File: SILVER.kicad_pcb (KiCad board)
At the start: 2 copper layers, 66 parts, among them J1 Conn_02x22, J2 Conn_02x22, J3 MPU6050, J4 MotorL, J5 motorR, J6 XT60-M, J7 STLINK, Q1 FCD600N60Z, Q2 FCD600N60Z, U1 VNH5019A-E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

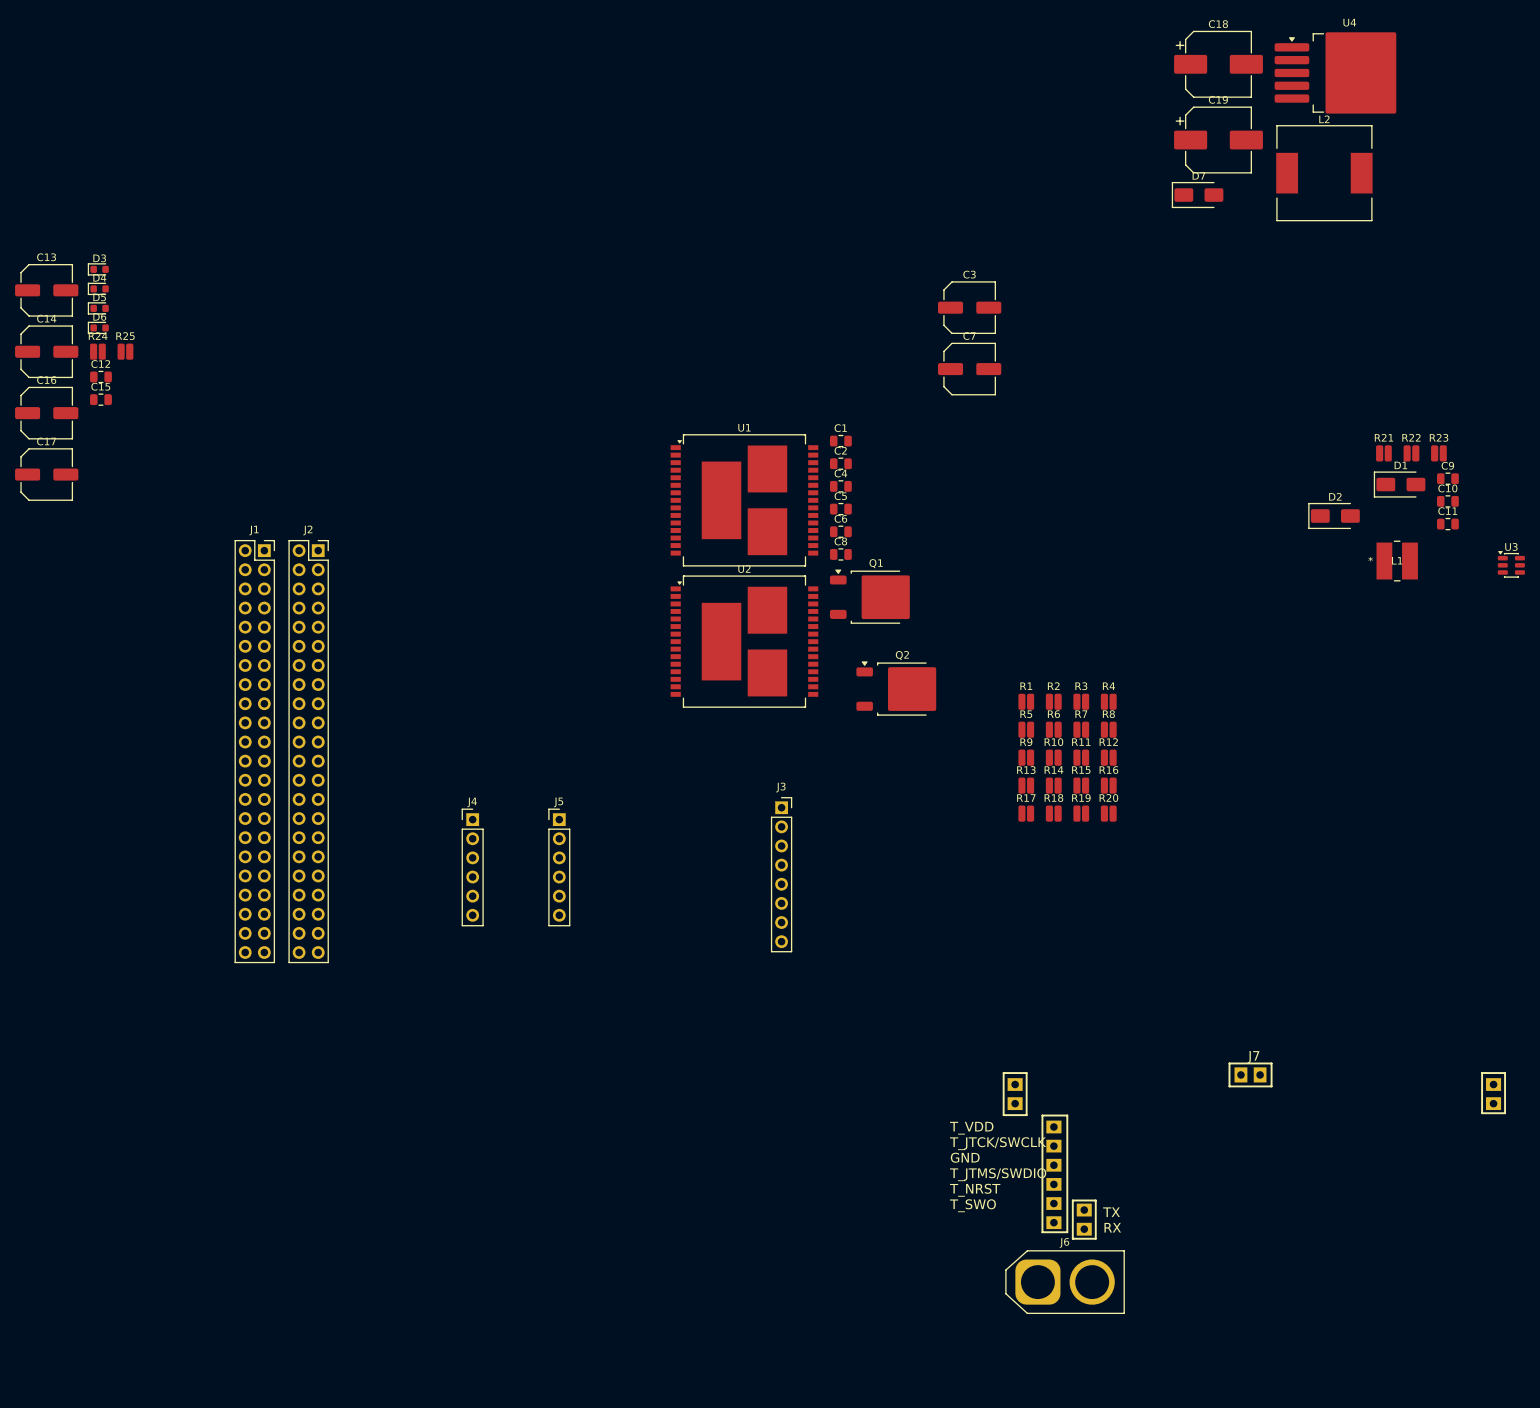
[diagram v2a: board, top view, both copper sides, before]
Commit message: feat: Update main project schematic and PCB with new component footprint and connector details, and add new RB141C1100 component files.
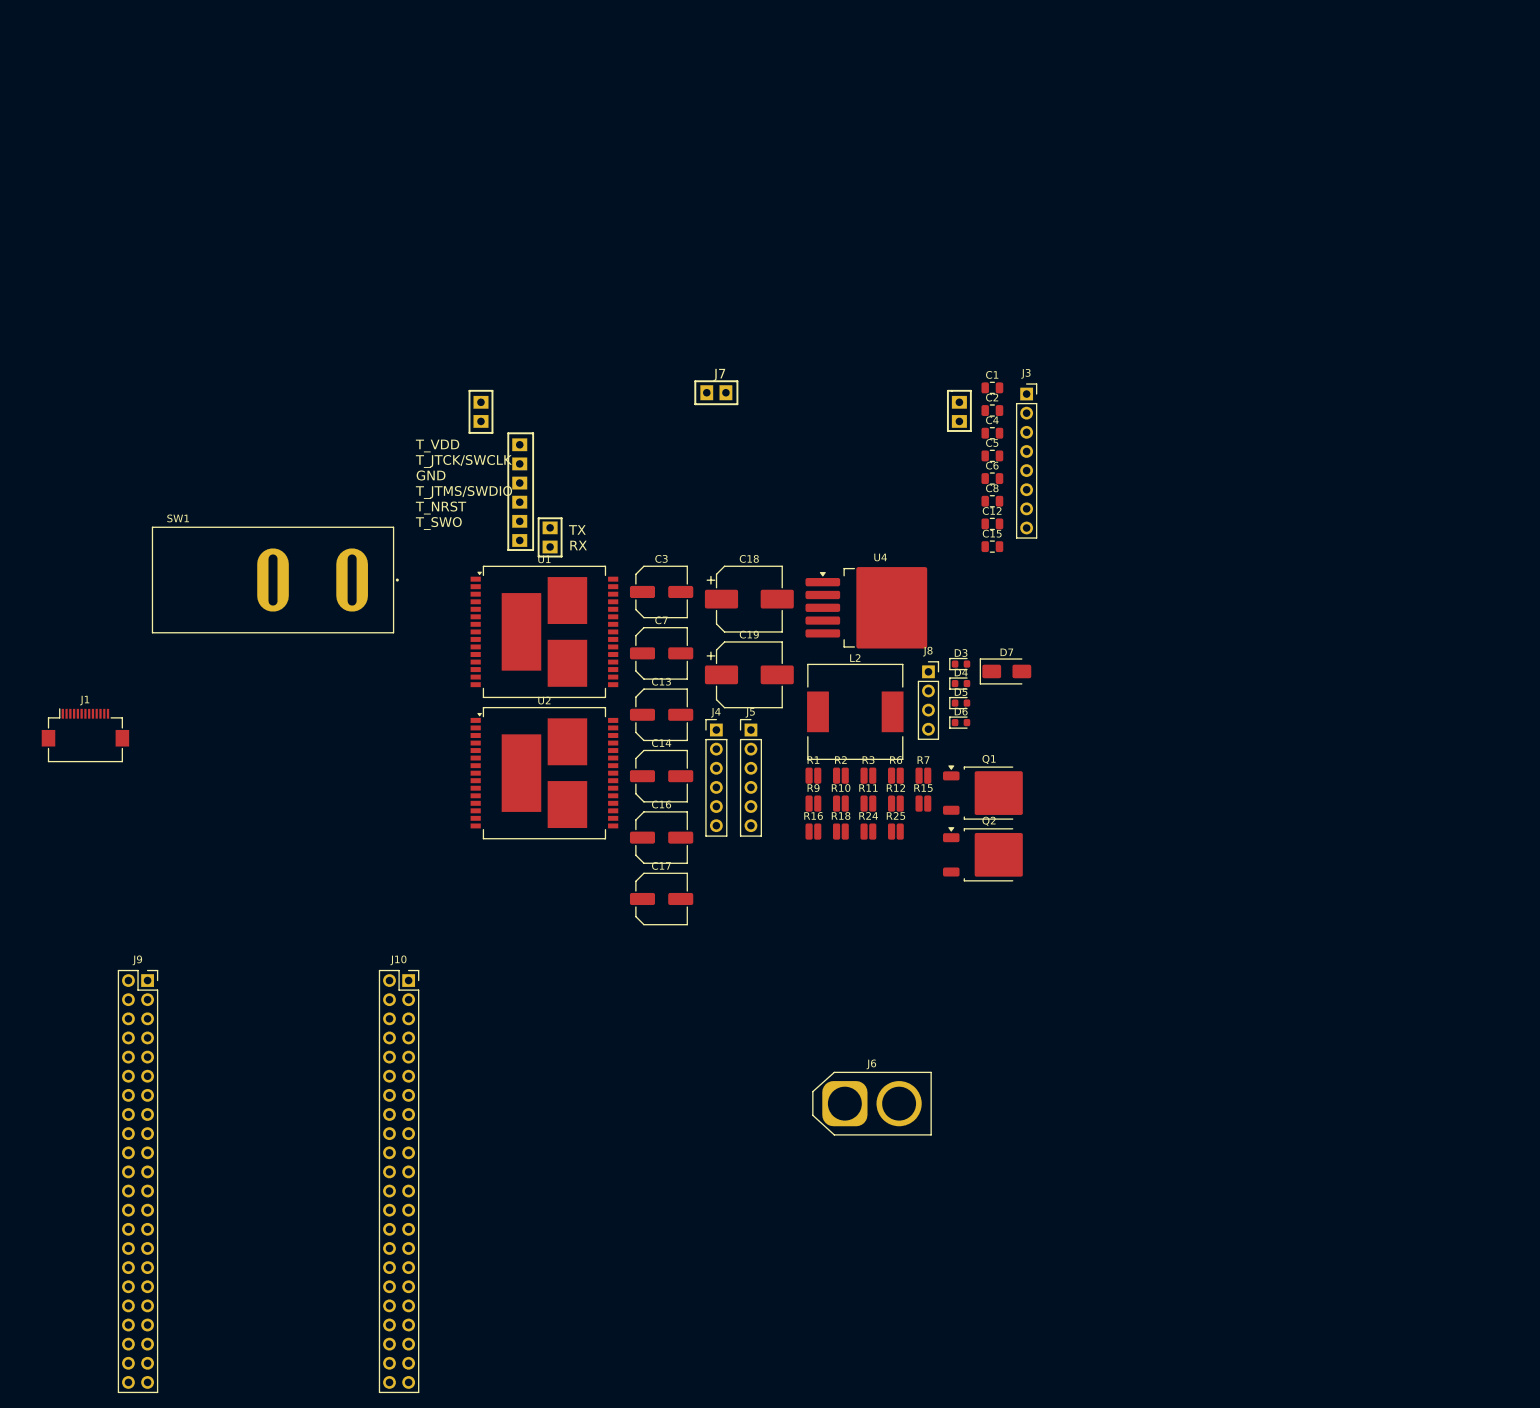
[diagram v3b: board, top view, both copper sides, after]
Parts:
- removed C10: 10nF, Capacitor_SMD:C_0805_2012Metric
- removed C11: 22uF 10v, Capacitor_SMD:C_0805_2012Metric
- removed C9: 10uF 25v, Capacitor_SMD:C_0805_2012Metric
- removed D1, D2: SS24, Diode_SMD:D_SMA
- removed J2: Conn_02x22, Connector_PinSocket_2.54mm:PinSocket_2x22_P2.54mm_Vertical
- removed L1: 4.7uH, Library:IND_5028_TDK
- removed R13, R14, R4, R5: 1k, Resistor_SMD:R_0508_1220Metric
- removed R17, R19, R20, R8: 4.7k, Resistor_SMD:R_0508_1220Metric
- removed R21: 100K, Resistor_SMD:R_0508_1220Metric
- removed R22: 49.9K, Resistor_SMD:R_0508_1220Metric
- removed R23: 9.53K, Resistor_SMD:R_0508_1220Metric
- removed U3: MP2359DJ-LF-Z, Package_TO_SOT_SMD:SOT-23-6
- added J10: Conn_02x22_Odd_Even_MountingPin, Connector_PinSocket_2.54mm:PinSocket_2x22_P2.54mm_Vertical, F.Cu at (80.0, 112.2)
- added J8: Conn_01x04_Pin, Connector_PinSocket_2.54mm:PinSocket_1x04_P2.54mm_Vertical, F.Cu at (149.0, 71.2)
- added J9: Conn_02x22_Odd_Even_MountingPin, Connector_PinSocket_2.54mm:PinSocket_2x22_P2.54mm_Vertical, F.Cu at (45.4, 112.2)
- added SW1: SW_DIP_x01, Library:SW_RB141C1100, F.Cu at (62.0, 59.0)
- J1: value Conn_02x22 -> Conn_01x13; footprint Connector_PinSocket_2.54mm:PinSocket_2x22_P2.54mm_Vertical -> Connector_FFC-FPC:Hirose_FH12-13S-0.5SH_1x13-1MP_P0.50mm_Horizontal
- J5: value motorR -> MotorR
- moved D3 125.8 mm to (153.3, 70.2)
- moved D4 125.8 mm to (153.3, 72.7)
- moved D5 125.8 mm to (153.3, 75.3)
- moved D6 125.8 mm to (153.3, 77.9)
- moved R25 120.5 mm to (144.7, 92.4)
- moved R24 120.5 mm to (141.0, 92.4)
- moved C12 119.9 mm to (157.5, 51.6)
- moved C15 119.9 mm to (157.5, 54.6)
- moved J7 115.0 mm to (121.4, 44.4)
- moved C13 99.2 mm to (113.6, 76.9)
- moved C14 99.2 mm to (113.6, 85.0)
- moved C16 99.2 mm to (113.6, 93.2)
- moved C17 99.2 mm to (113.6, 101.3)
- moved L2 94.8 mm to (139.3, 76.5)
- moved C18 94.4 mm to (125.2, 61.5)
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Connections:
- C1 pad 1: /A4_2 -> CS_R
- C12 pad 1: /12V -> +12V
- C19 pad 1: /VIN -> +12V
- C5 pad 1: /A4_2 -> CS_L
- C6 pad 2: /12V -> +12V
- D3 pad 2: /outa -> OUTA_L
- D4 pad 1: /outa -> OUTA_L
- D5 pad 1: /outa -> OUTA_R
- D6 pad 2: /outa -> OUTA_R
- J1 pad 1: (no net) -> C0
- J1 pad 10: (no net) -> B0
- J1 pad 11: (no net) -> B1
- J1 pad 12: (no net) -> +3.3V
- J1 pad 13: (no net) -> GND
- J1 pad 2: (no net) -> C1
- J1 pad 3: (no net) -> A0
- J1 pad 4: (no net) -> A1
- J1 pad 5: (no net) -> A4
- J1 pad 6: (no net) -> A6
- J1 pad 7: (no net) -> A7
- J1 pad 8: (no net) -> C4
- J1 pad 9: (no net) -> C5
- J3 pad 1: (no net) -> +3.3V
- J3 pad 2: (no net) -> GND
- J3 pad 3: (no net) -> B6
- J3 pad 4: (no net) -> B7
- J3 pad 5: (no net) -> XDA
- J3 pad 6: (no net) -> XCL
- J3 pad 7: (no net) -> ADD
- J3 pad 8: (no net) -> INT
- J4 pad 1: (no net) -> OUTA_L
- J4 pad 2: (no net) -> OUTB_L
- J4 pad 3: (no net) -> GND
- J4 pad 4: (no net) -> +3.3V
- J4 pad 5: (no net) -> B4
- J4 pad 6: (no net) -> B5
- J5 pad 1: (no net) -> OUTA_R
- J5 pad 2: (no net) -> OUTB_R
- J5 pad 3: (no net) -> GND
- J5 pad 4: (no net) -> +3.3V
- J5 pad 5: (no net) -> C7
- J5 pad 6: (no net) -> C6
- J6 pad 1: (no net) -> GND
- J6 pad 2: (no net) -> Net-(J6-+)
- J7 pad 201: (no net) -> +3.3V
- J7 pad 202: (no net) -> SWCLK
- J7 pad 203: (no net) -> GND
- J7 pad 204: (no net) -> SWDIO
- J7 pad 205: (no net) -> NR
- J7 pad 206: (no net) -> SWO
- J7 pad 207: (no net) -> TX
- J7 pad 208: (no net) -> RX
- Q1 pad 2: (no net) -> +12V
- Q2 pad 2: (no net) -> +12V
- R1 pad 2: /PWM -> D13
- R10 pad 2: /PWM -> D12
- R11 pad 1: /INA -> D11
- R12 pad 1: /INB -> D10
- R15 pad 1: /PWM -> D12
- R16 pad 2: /A4_2 -> CS_L
- R18 pad 1: /A4_2 -> CS_L
- R2 pad 1: /INA -> D9
- R24 pad 1: /outb -> OUTB_L
- R25 pad 1: /outb -> OUTB_R
- R3 pad 1: /INB -> D8
- R6 pad 1: /PWM -> D13
- R7 pad 2: /A4_2 -> CS_R
- R9 pad 1: /A4_2 -> CS_R
- U1 pad 16: /outb -> OUTB_R
- U1 pad 25: /outa -> OUTA_R
- U1 pad 6: unconnected-(U1-CS_DIS-Pad6) -> CS_DIS_R
- U2 pad 12: /12V -> +12V
- U2 pad 16: /outb -> OUTB_L
- U2 pad 25: /outa -> OUTA_L
- U2 pad 6: unconnected-(U2-CS_DIS-Pad6) -> CS_DIS_L
- U4 pad 1: /VIN -> +12V

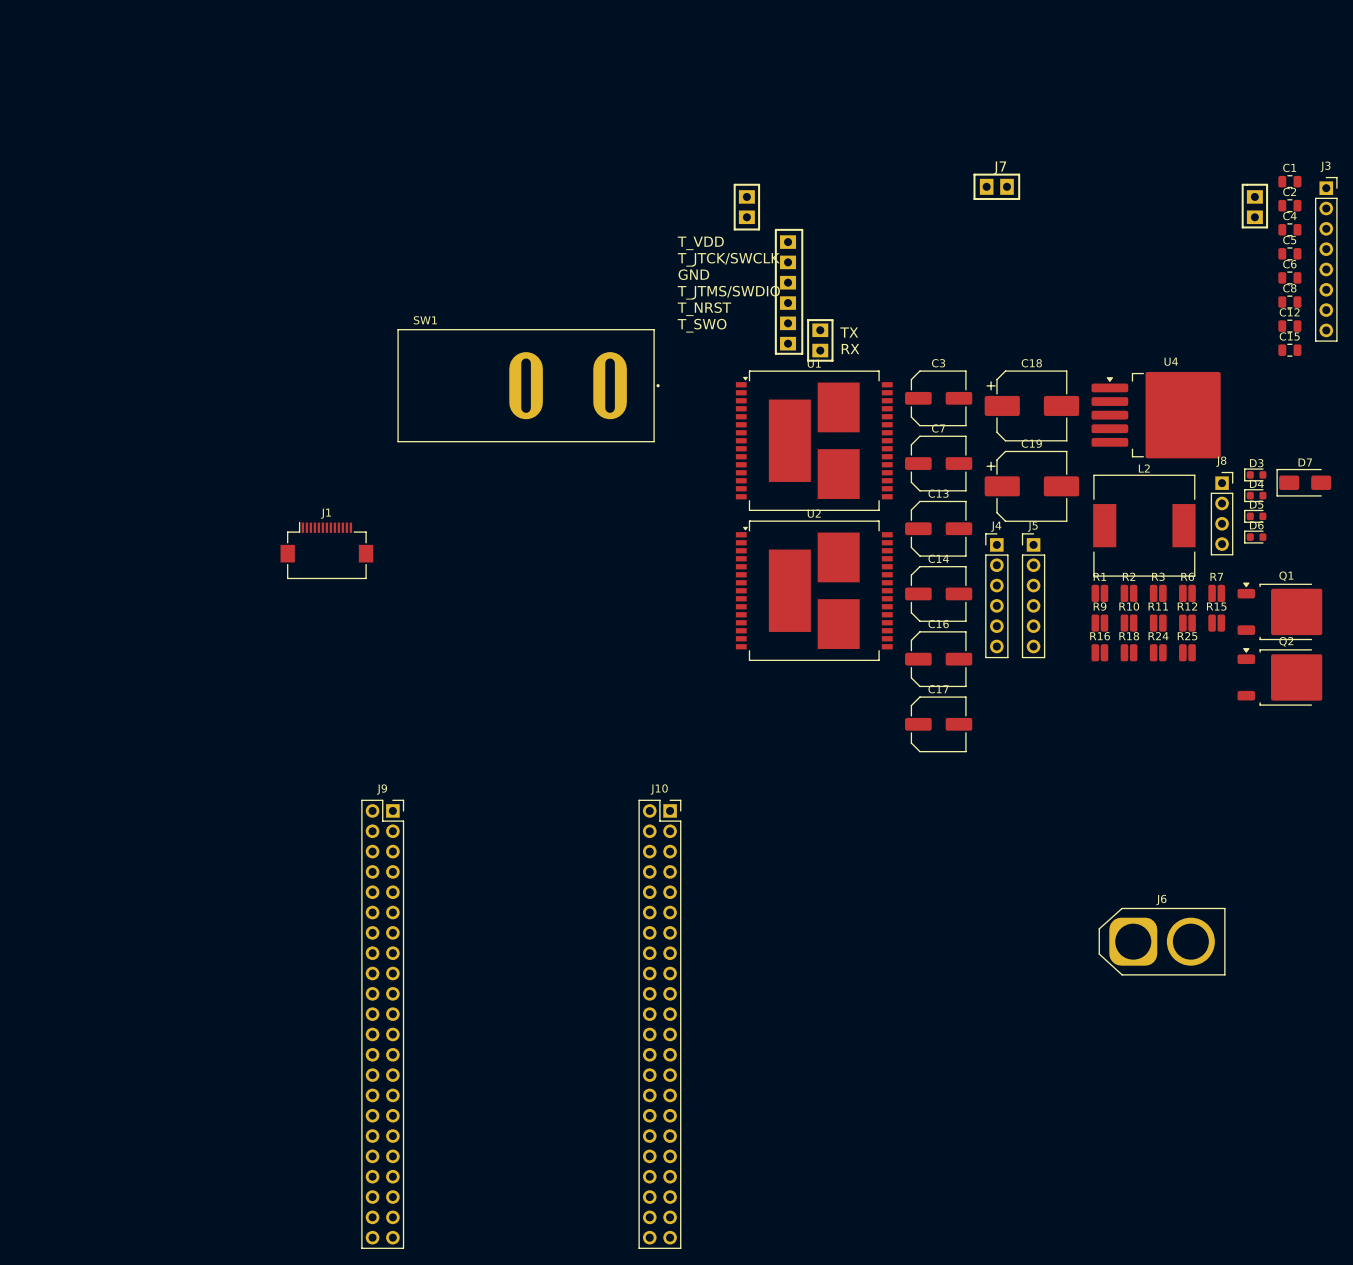
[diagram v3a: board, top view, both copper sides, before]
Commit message: Added ultrasonic sensor placement
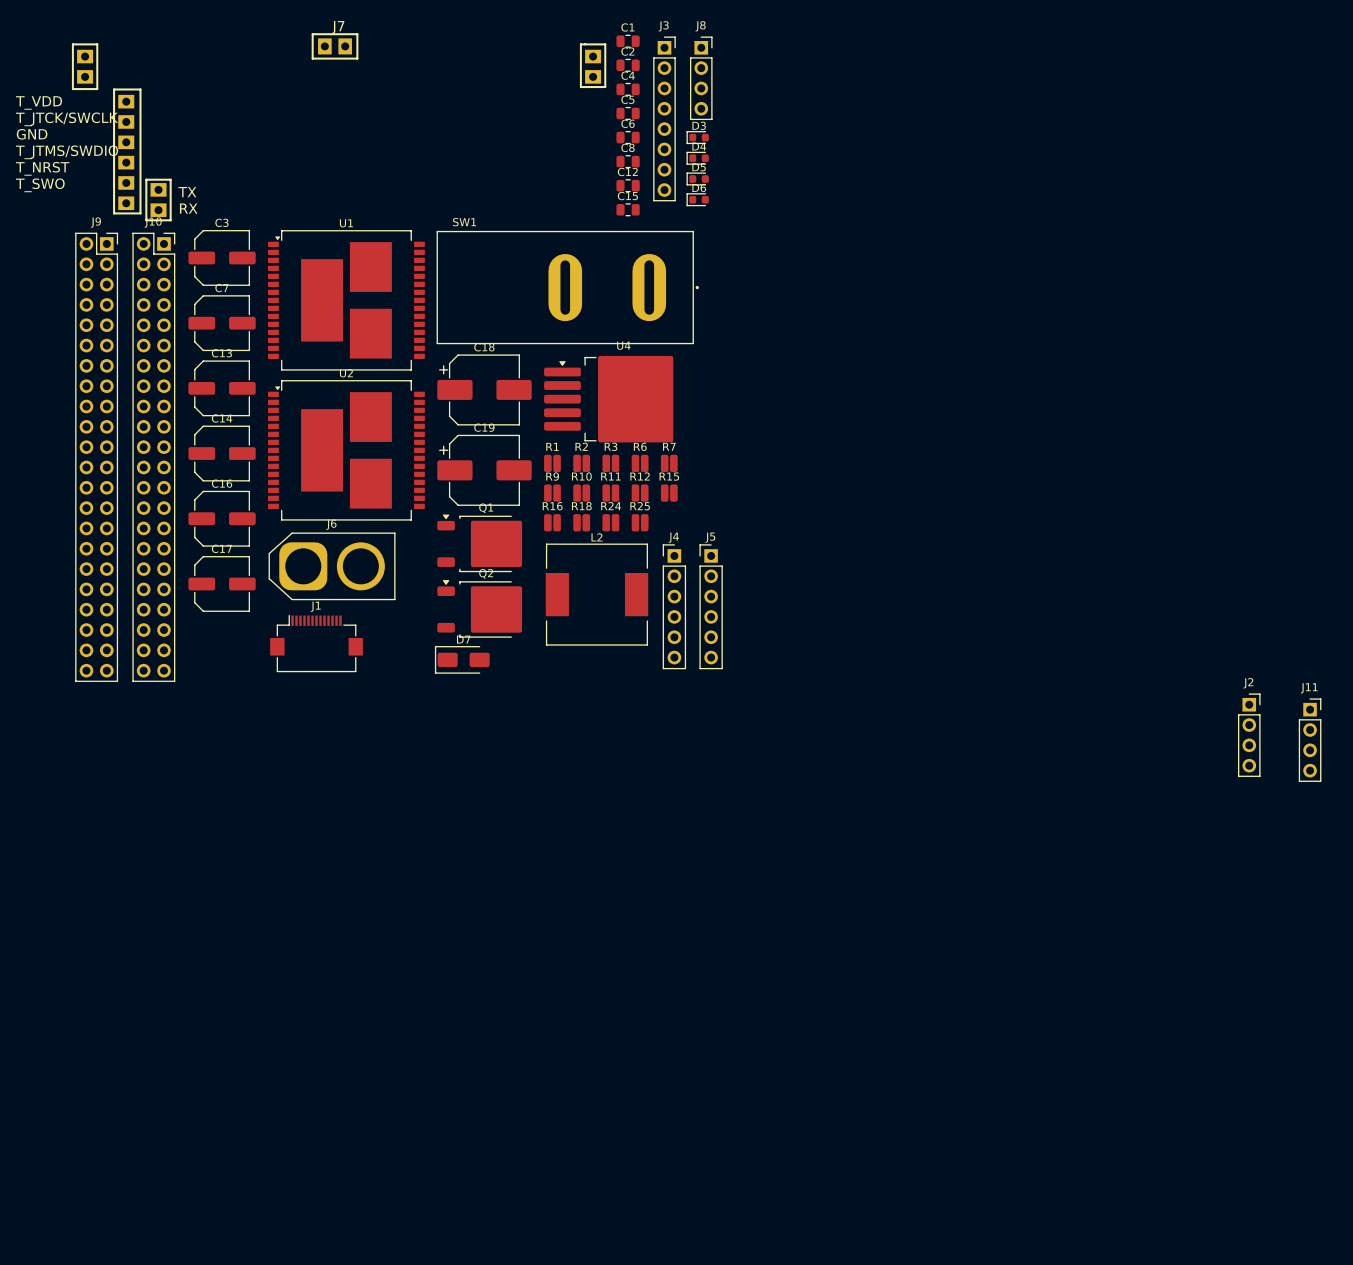
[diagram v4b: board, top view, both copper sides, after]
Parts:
- added J11: UltraRight, Connector_PinSocket_2.54mm:PinSocket_1x04_P2.54mm_Vertical, F.Cu at (160.0, 99.5)
- added J2: UltraLeft, Connector_PinSocket_2.54mm:PinSocket_1x04_P2.54mm_Vertical, F.Cu at (152.4, 98.9)
- moved J6 113.9 mm to (34.1, 81.6)
- moved D7 107.5 mm to (54.2, 93.3)
- moved Q1 100.4 mm to (57.0, 78.8)
- moved Q2 100.4 mm to (57.0, 87.0)
- moved J10 95.0 mm to (16.7, 41.3)
- moved C13 91.3 mm to (24.0, 59.3)
- moved C14 91.3 mm to (24.0, 67.5)
- moved C16 91.3 mm to (24.0, 75.6)
- moved C17 91.3 mm to (24.0, 83.8)
- moved C3 91.3 mm to (24.0, 43.0)
- moved C7 91.3 mm to (24.0, 51.2)
- moved J8 84.8 mm to (83.9, 16.8)
- moved J3 84.6 mm to (79.3, 16.8)
- moved C1 84.6 mm to (74.8, 15.9)
- moved C12 84.6 mm to (74.8, 34.0)
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
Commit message: added pcb outline
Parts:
- moved J10 207.0 mm to (219.0, 85.2)
- moved J9 179.4 mm to (183.5, 85.2)
- moved J2 120.9 mm to (31.9, 89.3)
- moved J11 119.3 mm to (41.1, 89.3)
- moved J8 86.6 mm to (36.5, 89.3)
- moved C13 35.4 mm to (55.7, 75.2)
- moved C3 35.4 mm to (55.7, 58.9)
- moved C14 35.4 mm to (55.7, 83.3)
- moved C16 35.4 mm to (55.7, 91.5)
- moved C17 35.4 mm to (55.7, 99.6)
- moved C7 35.4 mm to (55.7, 67.0)
- moved J1 31.8 mm to (67.5, 92.7)
- moved Q2 27.8 mm to (82.4, 98.4)
- moved Q1 27.8 mm to (82.4, 90.2)
- moved D6 16.0 mm to (94.2, 23.8)
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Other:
- board outline added: 120 x 80 mm
